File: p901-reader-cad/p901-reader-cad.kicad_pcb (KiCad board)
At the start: 2 copper layers, 91.3 x 97.4 mm, 20 parts, among them J1 DE15 (F), J2 5.5mm Barrel (F), U1 MAX232, U2 TPS63060, U3 DOIT ESP32 DevKit v1

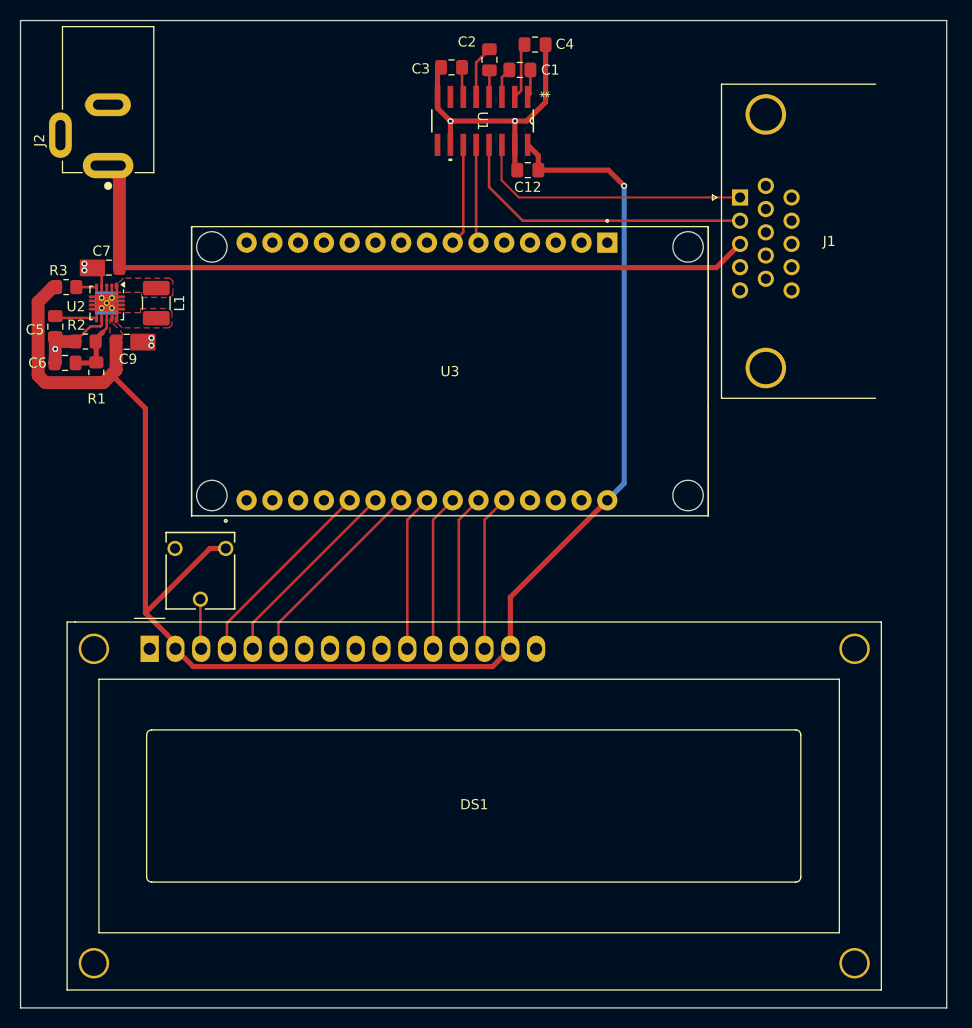
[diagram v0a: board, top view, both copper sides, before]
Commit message: redo the PCB since it kinda sucked
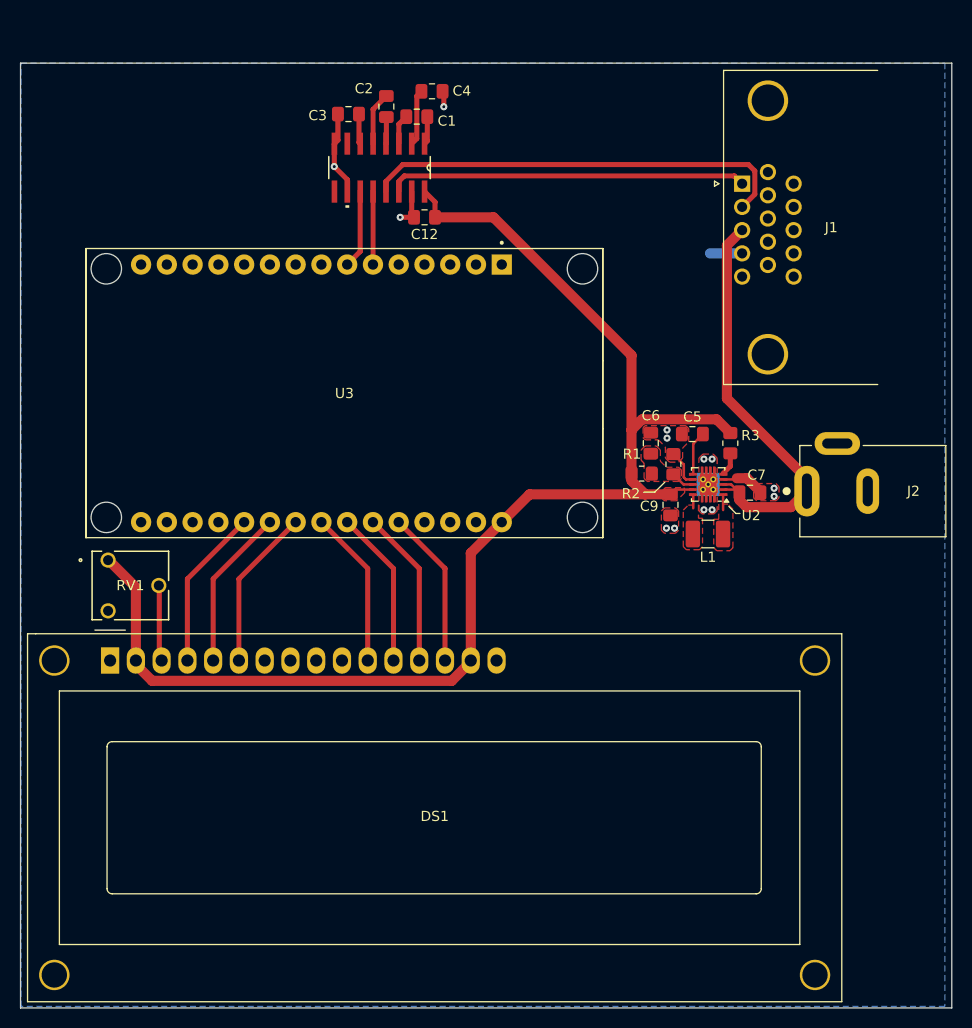
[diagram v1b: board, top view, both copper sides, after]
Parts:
- moved J2 76.0 mm to (162.8, 93.6), turned to 0 degrees
- moved R3 67.3 mm to (155.2, 88.9), turned to -90 degrees
- moved C7 67.0 mm to (157.2, 93.8), turned to 0 degrees
- moved C5 63.7 mm to (151.5, 88.0), turned to 180 degrees
- moved U2 61.9 mm to (153.1, 92.9), turned to 180 degrees
- moved R2 59.2 mm to (149.6, 90.9), turned to 90 degrees
- moved L1 59.0 mm to (153.0, 97.8), turned to 180 degrees
- moved C6 58.3 mm to (147.4, 88.9), turned to 90 degrees
- moved C9 56.0 mm to (149.3, 95.0), turned to -90 degrees
- moved R1 54.7 mm to (146.5, 91.9), turned to 0 degrees
- moved RV1 11.7 mm to (93.9, 100.4), turned to -90 degrees
- moved C12 11.2 mm to (125.1, 66.6)
- moved U1 11.2 mm to (120.7, 61.7)
- moved C1 11.2 mm to (124.3, 56.7)
- moved C2 11.2 mm to (121.3, 55.7)
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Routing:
- net +9V: track 72.7 -> 41.3 mm
- net +5V: track 158.0 -> 134.1 mm, vias 1 -> 0
- net GND: track 40.8 -> 25.5 mm, vias 7 -> 13
- net Net-(U1-R1IN): track 30.3 -> 42.4 mm
- net Net-(U1-T1OUT): track 28.6 -> 35.4 mm
- net Net-(U2-FB): track 6.19 -> 2.37 mm
- net /LCD_RW: track 19.7 -> 16.0 mm
- net /LCD_RS: track 19.7 -> 16.0 mm
- net /LCD_E: track 19.7 -> 16.0 mm
- net Net-(DS1-VO): track 4.93 -> 7.50 mm
- net /SER_IN: track 9.74 -> 7.20 mm
- net /SER_OUT: track 10.1 -> 7.73 mm
- net Net-(U2-L1): track 0.00 -> 1.52 mm
- net Net-(U2-L2): track 0.00 -> 1.35 mm
- net Net-(U2-VAUX): track 3.74 -> 4.36 mm
- added copper zone on B.Cu, net GND
- added copper zone on F.Cu, net GND
- added copper zone on F.Cu, net Net-(U2-FB)
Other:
- board size 91.3 x 97.4 mm -> 91.8 x 93.2 mm

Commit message: add via stitches, clean up random crap lying around
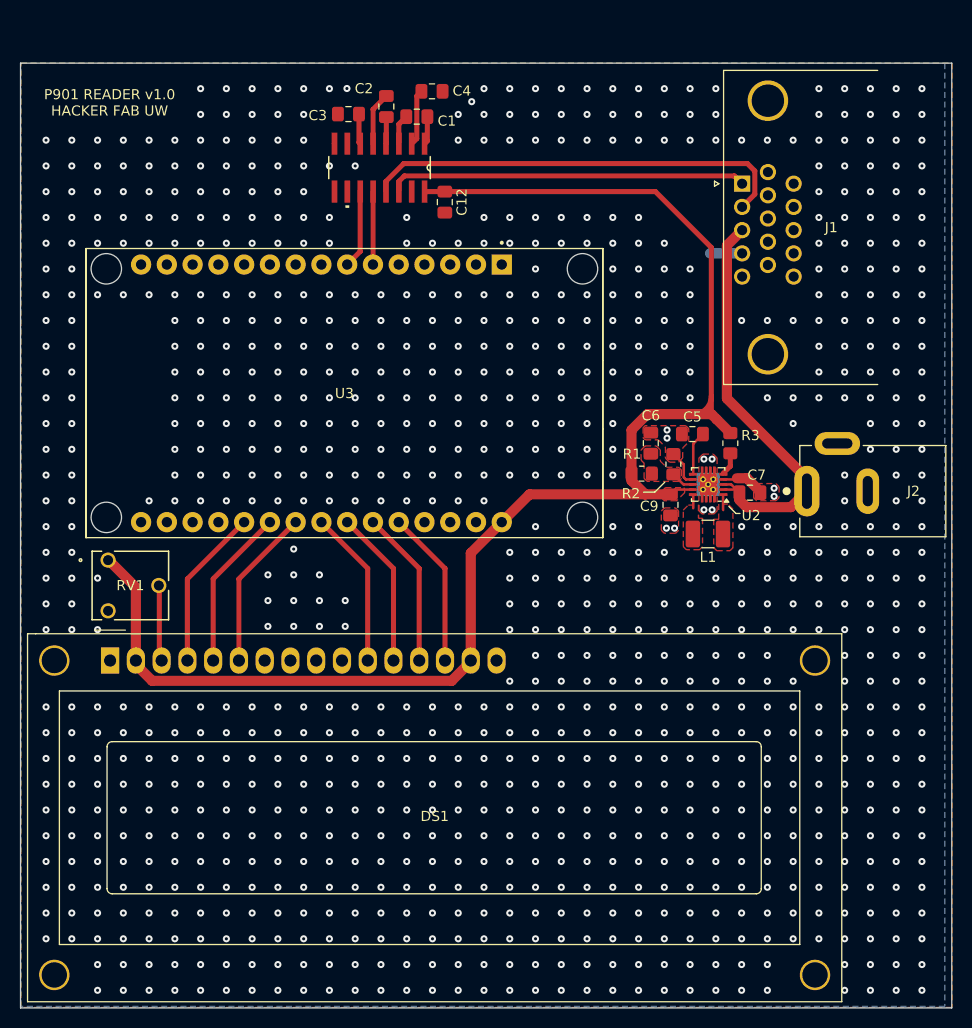
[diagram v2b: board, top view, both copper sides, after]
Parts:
- moved C12 2.50 mm to (127.1, 65.1), turned to -90 degrees
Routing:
- net GND: track 25.5 -> 11.8 mm, vias 13 -> 963
- net +5V: track 134.1 -> 146.9 mm
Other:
- board text added: "P901 READER v1.0 HACKER FAB UW"

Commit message: whoops missed some vias
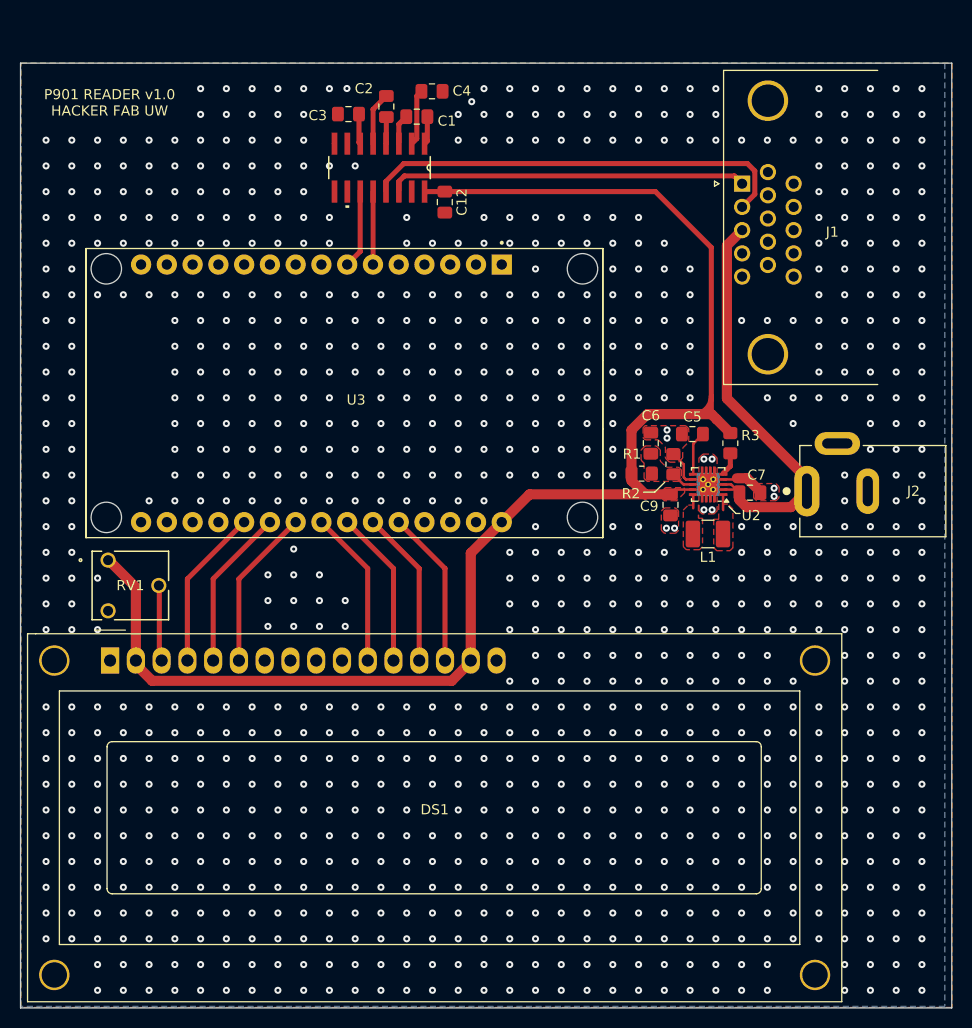
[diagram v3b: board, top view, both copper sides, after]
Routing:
- net GND: track 11.8 -> 8.63 mm, vias 963 -> 961
